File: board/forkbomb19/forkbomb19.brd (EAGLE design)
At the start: 100 x 100 mm, 30 parts, among them U1 ESP-WROOM-03

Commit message: drew the tv and started placing stuff
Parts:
- removed U$1: TLC59116-Q1, forkbomb19:TSSOP28
- added C10, C13, C14: 10uF, resistor:C1210
- added C11: 2.2uF, adafruit:C0805
- added C12: 0.1uF, adafruit:C0805
- added C62: 1F, resistor:E5-8,5
- added CHRG/LBO: ORANGE, piboy_new:ADAFRUIT_CHIPLED_0603
- added CN1: LIPO, adafruit:JST-PH-2-SMT-RA
- added D1: MBRS130LT3, diode:SMB
- added DONE: GREEN, piboy_new:ADAFRUIT_CHIPLED_0603
- added L1: 6.8uH, microbuilder:INDUCTOR_5X5MM_TDK_VLC5045
- added LBO: RED, piboy_new:ADAFRUIT_CHIPLED_0603
- added LOGO_B, LOGO_G, LOGO_R: (no value), forkbomb19:PLCC2_LED
- added ON: BLUE, piboy_new:ADAFRUIT_CHIPLED_0603
- added R10: 1.12M, resistor:R0603
- added R11: 200K, resistor:R0603
- added R12: 340K, adafruit:R0805
- added R13: 200K, adafruit:R0805
- added R14: 1.87M, adafruit:R0805
- added R15: 270K, resistor:R0603
- added R16, R21: 100K, resistor:R0603
- added R17, R18, R20, R9: 1K, resistor:R0603
- added R19: 1.0K, resistor:R0603
- added R22: 68, resistor:R0805
- added T3: MMUN2133LT1G, piboy_new:TRANSISTOR_SC59-BEC
- added THERM: 15K, resistor:R0603
- added U$17: CL-SB-12A-02T, defcon:CL-SB-12A-02T
- added U4: TPS61090RSAR, microbuilder:PVQFN-16
- added U5: MCP73871, microbuilder:QFN20_4MM
- C1: value (none) -> 100nF; device resistor:C0805 -> resistor:C0603
- C4, C9: device resistor:C0805 -> resistor:C0603
- R1, R6, R7: device resistor:R0805 -> resistor:R0603
- R8: value ILED -> 68
- moved R2 93.7 mm to (-8.49, 3.71)
- moved C9 91.0 mm to (-9.90, -9.40), flipped to the bottom, turned to 0 degrees
- moved C8 89.7 mm to (-10.4, -13.2), flipped to the bottom, turned to 0 degrees
- moved C4 87.1 mm to (-9.08, -4.52), flipped to the bottom
- moved C5 86.2 mm to (-20.4, 27.1), flipped to the bottom
- moved R1 75.4 mm to (3.94, 37.0), flipped to the bottom, turned to 270 degrees
- moved R8 69.6 mm to (72.1, 11.5), flipped to the bottom, turned to 270 degrees
- moved C1 64.2 mm to (10.4, 48.1), flipped to the bottom, turned to 180 degrees
- moved R7 63.9 mm to (3.37, 44.4), flipped to the bottom, turned to 90 degrees
- moved R6 63.0 mm to (6.15, 35.0), flipped to the bottom, turned to 270 degrees
- moved FID1 61.3 mm to (2.71, 2.32), flipped to the bottom
- moved U2 60.5 mm to (72.8, 16.5), turned to 90 degrees
- moved T2 59.4 mm to (4.96, 40.1), flipped to the bottom, turned to 270 degrees
- moved U3 59.3 mm to (8.31, 44.5), flipped to the bottom, turned to 270 degrees
- moved C2 57.0 mm to (13.5, 27.4), flipped to the bottom
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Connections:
- removed net RDY_2_SEND: U3.19
- new net BOOST_ENABLE: R13.2, U$17.P$2, U4.11
- new net LBO: T3.B, U4.12
- new net N$16: L1.P$2, U4.3, U4.4
- new net N$17: R12.2, R14.1, U4.9
- new net N$18: LBO.A, R20.1
- new net N$19: R10.1, R11.2, U4.14
- new net N$20: R20.2, T3.C
- new net N$21: ON.A, R9.2
- new net N$22: R15.1, R16.1, U5.P$2
- new net N$23: R18.1, U5.P$7
- new net N$24: R17.1, U5.P$8
- new net N$25: R19.2, U5.P$13
- new net N$26: THERM.2, U5.P$5
- new net N$27: DONE.C, R18.2
- new net N$28: CHRG/LBO.C, R17.2
- new net N$29: R21.2, U5.P$12
- new net N$30: CN1.1, D1.A
- new net N$31: LOGO_G.1, R8.2
- new net VBAT: C10.1, C12.1, L1.P$1, R13.1, R14.2, T3.E, U4.8, U5.P$1, U5.P$20
- new net VBUS: CHRG/LBO.A, DONE.A, R15.2, U5.P$17, U5.P$18, U5.P$19, U5.P$3, U5.P$4, U5.P$9
- new net VLIPO: C14.1, D1.C, U5.P$14, U5.P$15, U5.P$16
- net +3V3: now also C11.1, C13.1, C62.+, LOGO_B.1, R10.2, R22.1, R8.1, R9.1, U4.1, U4.15, U4.16; no longer U$1.P$28
- net EN: no longer U$1.P$25
- net GND: now also C10.2, C11.2, C12.2, C13.2, C14.2, C62.-, CN1.2, LBO.C, LOGO_B.2, LOGO_G.2, LOGO_R.2, ON.C, R11.1, R12.1, R16.2, R19.1, R21.1, THERM.1, U$17.P$3, U4.10, U4.13, U4.5, U4.6, U4.7, U4.P$18, U4.P$19, U4.P$20, U4.P$21, U4.P$22, U4.THERMAL, U5.P$10, U5.P$11, U5.P$21; no longer R8.1, U$1.P$10, U$1.P$19, U$1.P$2, U$1.P$24, U$1.P$3, U$1.P$4, U$1.P$5
- net I2C_SCL: no longer U$1.P$26
- net I2C_SDA: no longer U$1.P$27
- net N$12: now also LOGO_R.1, R22.2; no longer R8.2, U$1.P$1
- net RDY_2_SND: now also U3.19
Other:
- board size 100 x 100 mm -> 89.2 x 57 mm
- board text added: "COLOR"
- board text added: "FONY"
- board text added: "HACKATRON"
- board text added: "SOLID STATE"

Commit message: more layout work on the board
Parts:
- removed C13, C14: 10uF, resistor:C1210
- removed C62: 1F, resistor:E5-8,5
- removed CHRG/LBO: ORANGE, piboy_new:ADAFRUIT_CHIPLED_0603
- removed CN1: LIPO, adafruit:JST-PH-2-SMT-RA
- removed DONE: GREEN, piboy_new:ADAFRUIT_CHIPLED_0603
- removed LBO: RED, piboy_new:ADAFRUIT_CHIPLED_0603
- removed ON: BLUE, piboy_new:ADAFRUIT_CHIPLED_0603
- removed R12: 340K, adafruit:R0805
- removed R13: 200K, adafruit:R0805
- removed R14: 1.87M, adafruit:R0805
- removed R15: 270K, resistor:R0603
- removed R16, R21: 100K, resistor:R0603
- removed R17, R18, R20: 1K, resistor:R0603
- removed R19: 1.0K, resistor:R0603
- removed R2: 10K, pot:B64Y
- removed T3: MMUN2133LT1G, piboy_new:TRANSISTOR_SC59-BEC
- removed THERM: 15K, resistor:R0603
- removed U4: TPS61090RSAR, microbuilder:PVQFN-16
- removed U5: MCP73871, microbuilder:QFN20_4MM
- added D2: MBRS130LT3, diode:SMB
- added U$1: LM2623, forkbomb19:SSOP08
- added X2: 22-23-2021, con-molex:22-23-2021
- added X3: POT_GND, con-samtec:TSW-101-XX-G-S
- added X4: POT_3V3, con-samtec:TSW-101-XX-G-S
- added X5: POT_SIG, con-samtec:TSW-101-XX-G-S
- C10: value 10uF -> 22uF; device resistor:C1210 -> resistor:153CLV-0405
- C11: value 2.2uF -> 4.7pF; device adafruit:C0805 -> resistor:C0603
- C12: value 0.1uF -> 10uF; device adafruit:C0805 -> resistor:153CLV-0405
- L1: value 6.8uH -> 4.7uH; device microbuilder:INDUCTOR_5X5MM_TDK_VLC5045 -> resistor:POWER-CHOKE_WE-TPC
- R10: value 1.12M -> 165k
- R11: value 200K -> 100k
- R9: value 1K -> 150k
- moved C10 81.3 mm to (55.0, 42.0), turned to 270 degrees
- moved C8 79.5 mm to (64.6, 13.1)
- moved C9 79.0 mm to (65.1, 15.2)
- moved C11 72.8 mm to (49.6, 41.7), turned to 270 degrees
- moved C4 71.4 mm to (36.5, 50.3), turned to 180 degrees
- moved C5 61.2 mm to (37.0, 48.3), turned to 180 degrees
- moved U$17 57.8 mm to (61.1, 52.9), turned to 180 degrees
- moved D1 50.7 mm to (55.2, 35.0), turned to 270 degrees
- moved L1 47.0 mm to (49.8, 36.6), turned to 90 degrees
- moved R9 38.7 mm to (51.6, 41.7), turned to 270 degrees
- moved S1 35.6 mm to (27.0, 27.8), turned to 0 degrees
- moved C12 33.5 mm to (50.7, 51.0), turned to 0 degrees
- moved R11 30.6 mm to (55.7, 47.0), turned to 90 degrees
- moved R10 26.1 mm to (53.7, 47.0), turned to 270 degrees
- moved R1 7.98 mm to (9.39, 42.8), turned to 180 degrees
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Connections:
- net SCRN_D0 renamed SCRN_CLK
- net SCRN_D1 renamed SCRN_MOSI
- net SCRN_D3 renamed TSCRN_X2
- net SCRN_D4 renamed TSCRN_X1
- net SCRN_D5 renamed TSCRN_Y2
- net SCRN_D6 renamed TSCRN_Y1
- net SCRN_D7 renamed SCRN_MISO
- removed net BOOST_ENABLE: R13.2, U$17.P$2, U4.11
- removed net LBO: T3.B, U4.12
- removed net N$19: R10.1, R11.2, U4.14
- removed net N$20: R20.2, T3.C
- removed net N$21: ON.A, R9.2
- removed net N$22: R15.1, R16.1, U5.P$2
- removed net N$23: R18.1, U5.P$7
- removed net N$24: R17.1, U5.P$8
- removed net N$25: R19.2, U5.P$13
- removed net N$26: THERM.2, U5.P$5
- removed net N$27: DONE.C, R18.2
- removed net N$28: CHRG/LBO.C, R17.2
- removed net N$29: R21.2, U5.P$12
- removed net SCRN_D2: U1.16
- removed net SCRN_RDX: U1.29
- removed net SCRN_WRX: U1.28
- removed net VBAT: C10.1, C12.1, L1.P$1, R13.1, R14.2, T3.E, U4.8, U5.P$1, U5.P$20
- removed net VBUS: CHRG/LBO.A, DONE.A, R15.2, U5.P$17, U5.P$18, U5.P$19, U5.P$3, U5.P$4, U5.P$9
- removed net VLIPO: C14.1, D1.C, U5.P$14, U5.P$15, U5.P$16
- new net N$13: C10.+, D1.C, L1.1, R9.2
- new net N$14: C11.2, R9.1, U$1.3
- new net N$15: C11.1, D2.A, L1.2, U$1.8
- new net SCRN_RST: U1.30
- net +3V3: now also C12.+, D2.C, X4.1; no longer C11.1, C13.1, C62.+, R10.2, R2.A, R9.1, U4.1, U4.15, U4.16
- net GND: now also C10.-, C12.-, U$1.1, U$1.5, U$17.P$1, X2.2, X3.1; no longer C10.2, C11.2, C12.2, C13.2, C14.2, C62.-, CN1.2, LBO.C, ON.C, R12.1, R16.2, R19.1, R2.E, R21.1, THERM.1, U$17.P$3, U4.10, U4.13, U4.5, U4.6, U4.7, U4.P$18, U4.P$19, U4.P$20, U4.P$21, U4.P$22, U4.THERMAL, U5.P$10, U5.P$11, U5.P$21
- net N$16: now also R10.2, U$1.6, U$1.7, U$17.P$3; no longer L1.P$2, U4.3, U4.4
- net N$17: now also U$1.2, U$17.P$2; no longer R12.2, R14.1, U4.9
- net N$18: now also R10.1, R11.2, U$1.4; no longer LBO.A, R20.1
- net N$30: now also X2.1; no longer CN1.1
- net N$4: now also X5.1; no longer R2.S
- net SCRN_CSX: now also U1.28; no longer U1.30
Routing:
- net +3V3: track 0.00 -> 73.5 mm, vias 0 -> 3
- net EN: track 0.00 -> 33.8 mm, vias 0 -> 4
- net N$16: track 0.00 -> 27.1 mm
- net UART_RX: track 0.00 -> 17.7 mm
- net N$30: track 0.00 -> 16.1 mm
- net N$1: track 0.00 -> 15.9 mm, vias 0 -> 2
- net UART_TX: track 0.00 -> 15.7 mm
- net N$3: track 0.00 -> 14.9 mm, vias 0 -> 2
- net N$13: track 0.00 -> 14.3 mm
- net GPIO0: track 0.00 -> 12.9 mm
- net N$17: track 0.00 -> 12.4 mm
- net N$15: track 0.00 -> 12.1 mm
- net +5V: track 0.00 -> 10.1 mm, vias 0 -> 2
- net RDY_2_SND: track 0.00 -> 8.44 mm, vias 0 -> 2
- net N$14: track 0.00 -> 5.35 mm, vias 0 -> 2
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
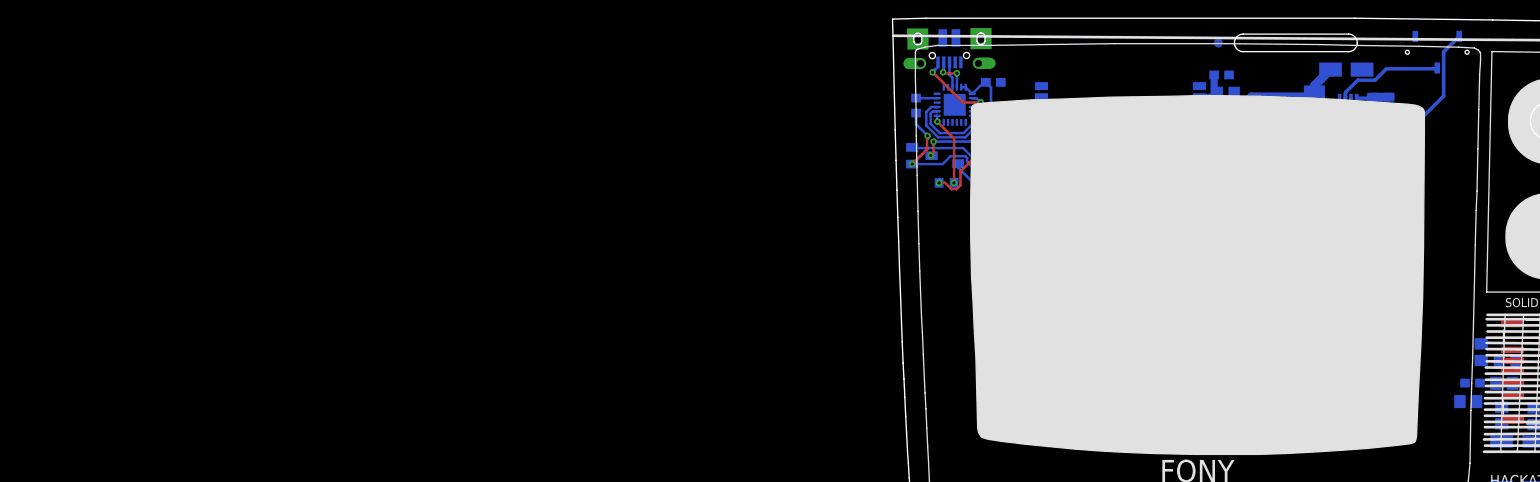
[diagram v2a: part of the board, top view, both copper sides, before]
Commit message: better layout, made room for AA's
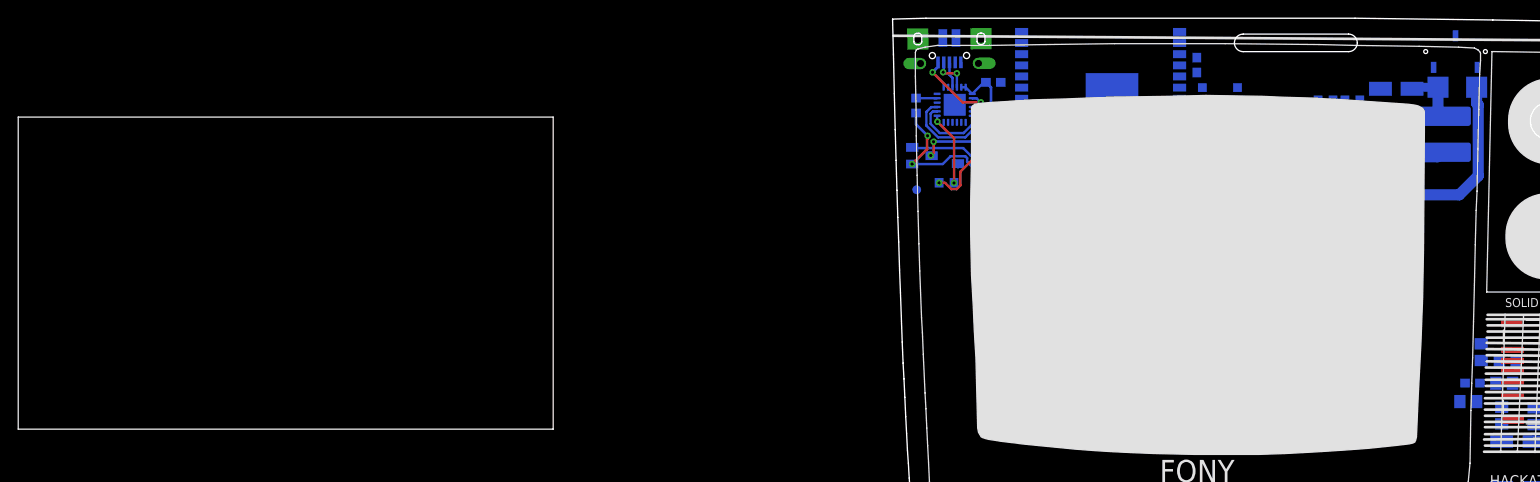
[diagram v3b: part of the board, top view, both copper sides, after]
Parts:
- removed S1: SFT_RST, SparkFun-Switches:TACTILE_SWITCH_SMD_6.0X3.5MM
- added SW1: SPST_TACT-KMR2, adafruit:KMR2
- moved FID4 38.2 mm to (1.80, 37.3)
- moved JP1 28.6 mm to (10.3, 36.3)
- moved D1 16.2 mm to (63.4, 48.9), turned to 180 degrees
- moved L1 13.9 mm to (61.8, 43.6), turned to 0 degrees
- moved X2 10.9 mm to (53.4, 36.7), turned to 180 degrees
- moved C12 8.05 mm to (46.7, 44.0)
- moved D2 7.36 mm to (52.7, 40.9), turned to 180 degrees
- moved C11 7.33 mm to (56.7, 43.4), turned to 180 degrees
- moved R11 7.33 mm to (48.4, 47.4), turned to 180 degrees
- moved C10 6.96 mm to (56.4, 48.8), turned to 180 degrees
- moved U1 6.57 mm to (22.8, 47.5)
- moved R9 6.30 mm to (56.7, 45.4), turned to 180 degrees
- moved C2 6.03 mm to (16.7, 33.8)
- moved C5 5.07 mm to (33.9, 44.3), turned to 270 degrees
- moved C4 3.05 mm to (33.7, 51.5), turned to 270 degrees
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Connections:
- net GND: now also SW1.2, SW1.4; no longer S1.2
- net N$2: now also SW1.1, SW1.3; no longer S1.1
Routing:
- net +3V3: track 73.5 -> 17.7 mm, vias 3 -> 2
- net EN: track 33.8 -> 6.61 mm, vias 4 -> 2
- net N$16: track 27.1 -> 5.31 mm
- net GPIO0: track 12.9 -> 0.43 mm
- net N$17: track 12.4 -> 0.00 mm
- net UART_TX: track 15.7 -> 8.39 mm
- net UART_RX: track 17.7 -> 10.6 mm
- net N$30: track 16.1 -> 22.1 mm
- net N$14: track 5.35 -> 8.15 mm
- net N$15: track 12.1 -> 12.9 mm

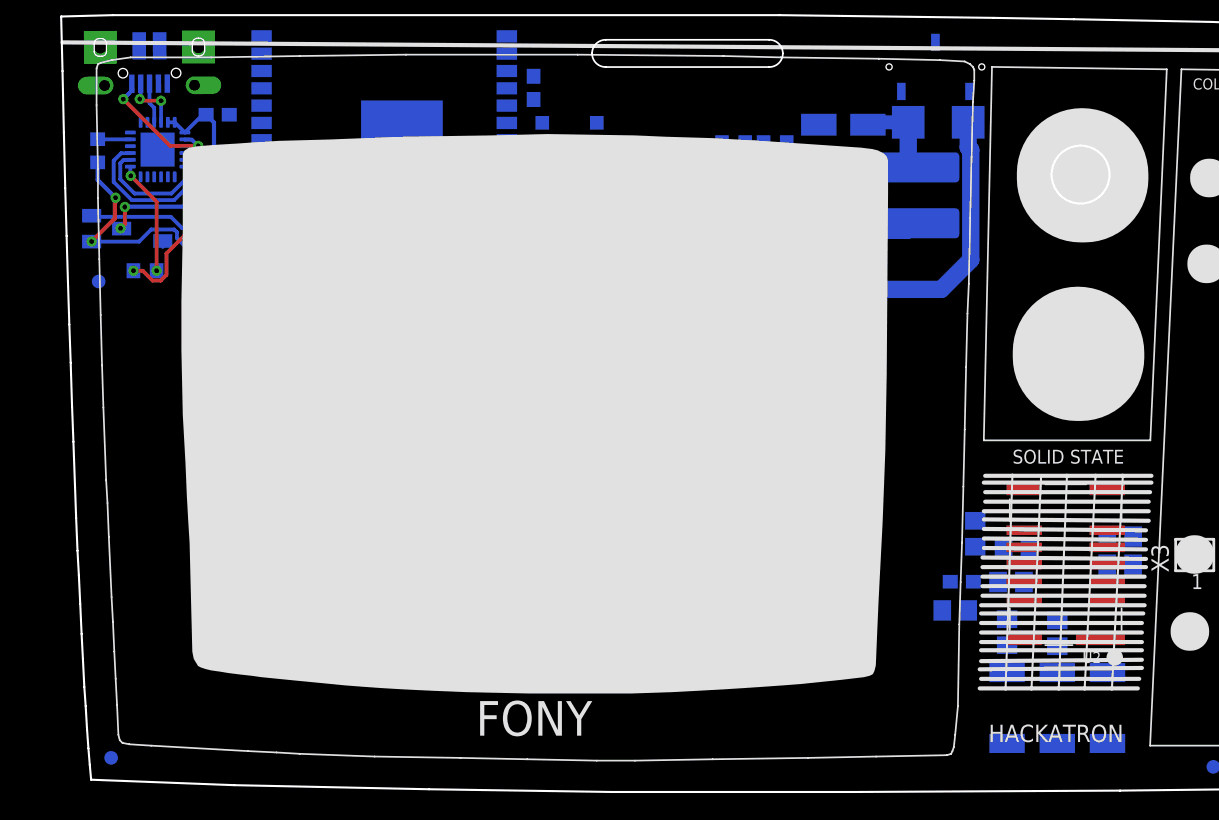
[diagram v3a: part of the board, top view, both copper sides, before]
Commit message: more layout work, trying to remove excess vias
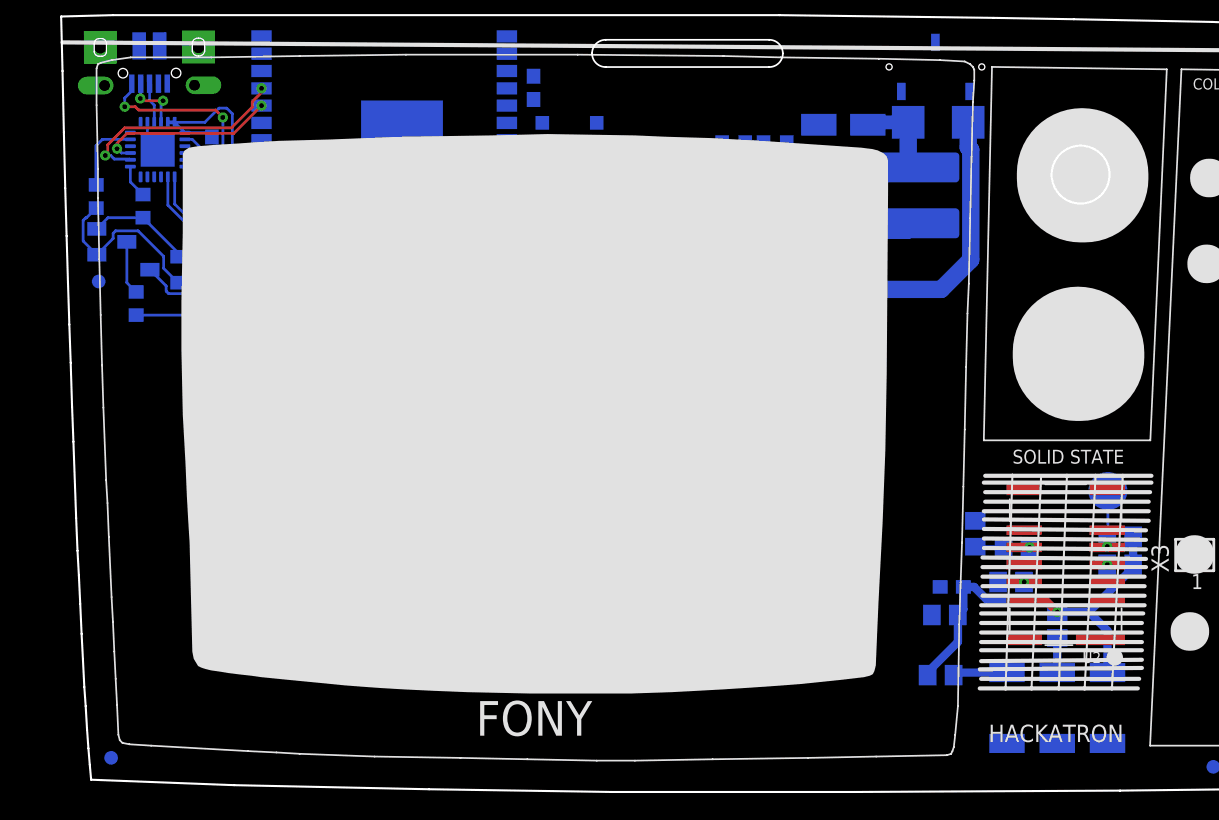
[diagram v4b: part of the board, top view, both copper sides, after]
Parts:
- added JP2: (no value), SparkFun-Jumpers:SMT-JUMPER_2_NO_SILK_ROUND
- added LED1, LED2: (no value), led:SML0603
- added R12, R2: 300, resistor:R0603
- moved JP1 15.2 mm to (25.3, 34.2)
- moved R1 8.66 mm to (4.55, 35.6), turned to 270 degrees
- moved R22 5.81 mm to (63.6, 8.38), turned to 180 degrees
- moved R6 4.74 mm to (5.05, 42.8), turned to 90 degrees
- moved R7 3.35 mm to (1.62, 43.5)
- moved C1 2.52 mm to (10.1, 47.0), turned to 270 degrees
- moved T1 2.31 mm to (6.66, 38.1)
- moved T2 1.04 mm to (2.76, 40.2)
- moved C8 0.83 mm to (63.9, 12.8)
- moved C9 0.83 mm to (64.4, 14.9)
- moved R8 0.61 mm to (72.1, 12.1)
- turned LOGO_B to 270 degrees
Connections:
- new net N$19: LED2.C, U3.13
- new net N$20: LED1.C, U3.14
- new net N$21: LED1.A, R2.2
- new net N$22: LED2.A, R12.2
- net +3V3: now also R12.1, R2.1
- net GND: now also JP2.1
- net N$7: now also JP2.2
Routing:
- net +3V3: track 17.7 -> 70.8 mm, vias 2 -> 3
- net GPIO0: track 0.43 -> 11.2 mm
- net +5V: track 10.1 -> 18.0 mm
- net UART_TX: track 8.39 -> 16.2 mm, vias 0 -> 2
- net N$19: track 0.00 -> 7.65 mm
- net N$20: track 0.00 -> 7.04 mm
- net N$3: track 14.9 -> 8.04 mm, vias 2 -> 0
- net RDY_2_SND: track 8.44 -> 2.43 mm, vias 2 -> 0
- net N$12: track 0.00 -> 4.00 mm
- net DAT_TERM_RDY: track 2.41 -> 5.61 mm
- net UART_RX: track 10.6 -> 13.7 mm, vias 0 -> 2
- net GND: track 0.00 -> 2.93 mm, vias 0 -> 1
- net N$7: track 0.00 -> 2.89 mm, vias 0 -> 1
- net EN: track 6.61 -> 3.96 mm, vias 2 -> 0
- net N$31: track 0.00 -> 2.55 mm
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
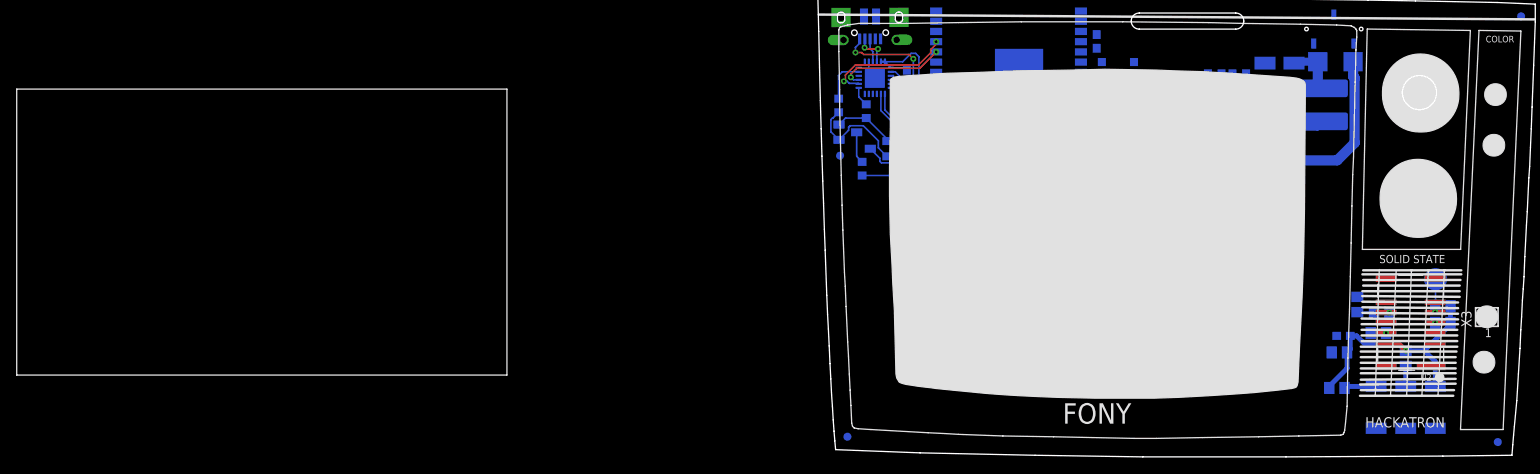
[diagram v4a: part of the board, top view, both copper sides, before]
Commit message: silkscreen placement
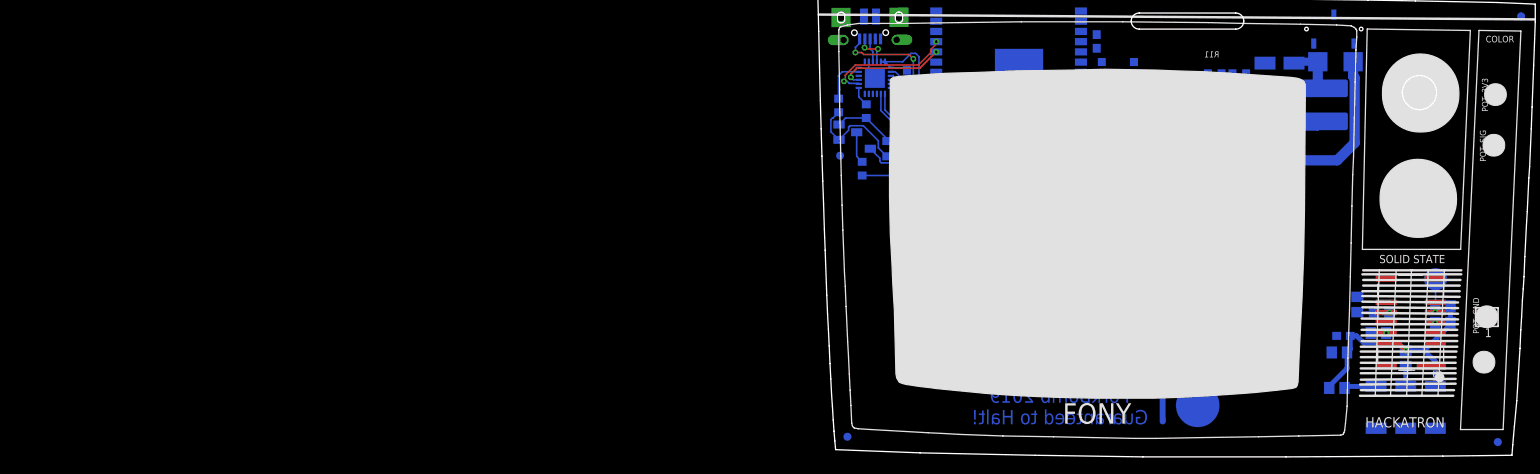
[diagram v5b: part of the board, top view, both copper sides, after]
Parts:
- renumbered JP1 to HRDRST, JP2 to ADDR, LED1 to TX, LED2 to RX, X2 to BATT
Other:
- board text added: "+"
- board text added: "-"
- board text added: "B"
- board text added: "G"
- board text added: "R"
- board text added: "while(1){fork();} ForkBomb 2019 Guaranteed to Halt!"
